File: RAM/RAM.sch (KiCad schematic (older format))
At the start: 27 parts, among them J1 Conn_01x08_Male, J2 Conn_01x08_Male, J3 Conn_01x08_Male, J4 Conn_01x05_Male, J5 Conn_01x08_Male, U1 74LS283, U2 CY62256-70PC, U3 74LS283, U4 74LS283, U5 74LS283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

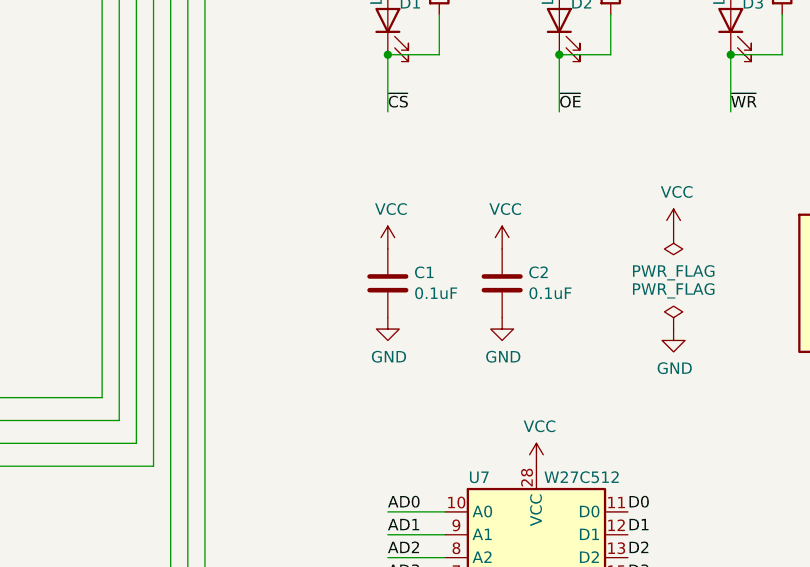
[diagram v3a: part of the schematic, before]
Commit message: Polishing RAM & ROM
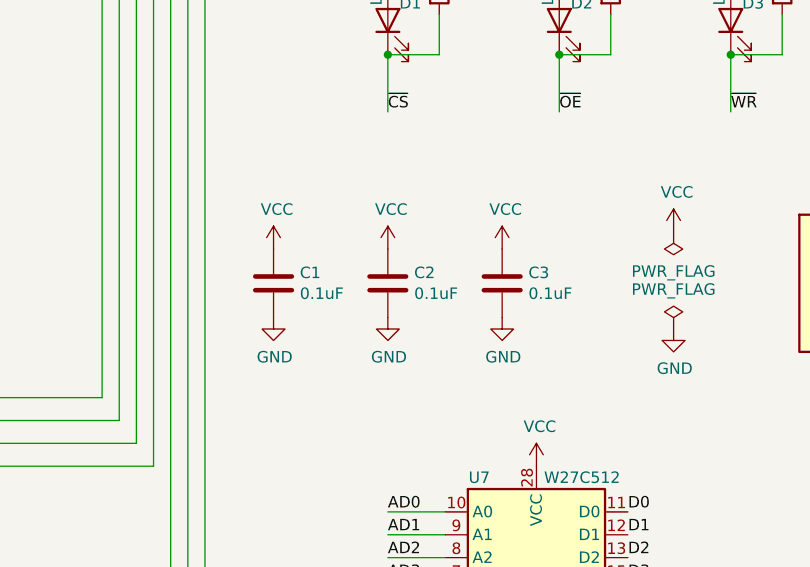
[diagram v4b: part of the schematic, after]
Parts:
- added C3: 0.1uF, Capacitor_THT:C_Disc_D7.5mm_W5.0mm_P10.00mm, symbol Device:C
- C1: footprint Resistor_SMD:R_0805_2012Metric_Pad1.20x1.40mm_HandSolder -> Capacitor_THT:C_Disc_D7.5mm_W5.0mm_P10.00mm
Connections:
- net GND: now also C3.2
- net VCC: now also C3.1
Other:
- moved on the sheet: C1, C2
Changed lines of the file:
@@
 L power:VCC #PWR012
 U 1 1 63DCFBC2
-P 5000 5100
-F 0 "#PWR012" H 5000 4950 50  0001 C CNN
-F 1 "VCC" H 5015 5273 50  0000 C CNN
-F 2 "" H 5000 5100 50  0001 C CNN
-F 3 "" H 5000 5100 50  0001 C CNN
-	1    5000 5100
+P 4500 5100
+F 0 "#PWR012" H 4500 4950 50  0001 C CNN
+F 1 "VCC" H 4515 5273 50  0000 C CNN
+F 2 "" H 4500 5100 50  0001 C CNN
+F 3 "" H 4500 5100 50  0001 C CNN
+	1    4500 5100
 	1    0    0    -1
 $EndComp
@@
 L power:GND #PWR013
 U 1 1 63DD055E
-P 5000 5400
-F 0 "#PWR013" H 5000 5150 50  0001 C CNN
-F 1 "GND" H 5005 5227 50  0000 C CNN
-F 2 "" H 5000 5400 50  0001 C CNN
-F 3 "" H 5000 5400 50  0001 C CNN
-	1    5000 5400
+P 4500 5400
+F 0 "#PWR013" H 4500 5150 50  0001 C CNN
+F 1 "GND" H 4505 5227 50  0000 C CNN
+F 2 "" H 4500 5400 50  0001 C CNN
+F 3 "" H 4500 5400 50  0001 C CNN
+	1    4500 5400
 	1    0    0    -1
 $EndComp
@@
 L Device:C C1
 U 1 1 63DD1002
-P 5000 5250
-F 0 "C1" H 5115 5296 50  0000 L CNN
-F 1 "0.1uF" H 5115 5205 50  0000 L CNN
-F 2 "Resistor_SMD:R_0805_2012Metric_Pad1.20x1.40mm_HandSolder" H 5038 5100 50  0001 C CNN
-F 3 "~" H 5000 5250 50  0001 C CNN
-	1    5000 5250
+P 4500 5250
+F 0 "C1" H 4615 5296 50  0000 L CNN
+F 1 "0.1uF" H 4615 5205 50  0000 L CNN
+F 2 "Capacitor_THT:C_Disc_D7.5mm_W5.0mm_P10.00mm" H 4538 5100 50  0001 C CNN
+F 3 "~" H 4500 5250 50  0001 C CNN
+	1    4500 5250
 	1    0    0    -1
 $EndComp
@@
 L power:VCC #PWR018
 U 1 1 63E17CDB
-P 5500 5100
-F 0 "#PWR018" H 5500 4950 50  0001 C CNN
-F 1 "VCC" H 5515 5273 50  0000 C CNN
-F 2 "" H 5500 5100 50  0001 C CNN
-F 3 "" H 5500 5100 50  0001 C CNN
-	1    5500 5100
+P 5000 5100
+F 0 "#PWR018" H 5000 4950 50  0001 C CNN
+F 1 "VCC" H 5015 5273 50  0000 C CNN
+F 2 "" H 5000 5100 50  0001 C CNN
+F 3 "" H 5000 5100 50  0001 C CNN
+	1    5000 5100
 	1    0    0    -1
 $EndComp
@@
 L power:GND #PWR019
 U 1 1 63E17CE1
-P 5500 5400
-F 0 "#PWR019" H 5500 5150 50  0001 C CNN
-F 1 "GND" H 5505 5227 50  0000 C CNN
-F 2 "" H 5500 5400 50  0001 C CNN
-F 3 "" H 5500 5400 50  0001 C CNN
-	1    5500 5400
+P 5000 5400
+F 0 "#PWR019" H 5000 5150 50  0001 C CNN
+F 1 "GND" H 5005 5227 50  0000 C CNN
+F 2 "" H 5000 5400 50  0001 C CNN
+F 3 "" H 5000 5400 50  0001 C CNN
+	1    5000 5400
 	1    0    0    -1
 $EndComp
@@
 L Device:C C2
 U 1 1 63E17CE7
-P 5500 5250
-F 0 "C2" H 5615 5296 50  0000 L CNN
-F 1 "0.1uF" H 5615 5205 50  0000 L CNN
-F 2 "Capacitor_THT:C_Disc_D7.5mm_W5.0mm_P10.00mm" H 5538 5100 50  0001 C CNN
-F 3 "~" H 5500 5250 50  0001 C CNN
-	1    5500 5250
+P 5000 5250
+F 0 "C2" H 5115 5296 50  0000 L CNN
+F 1 "0.1uF" H 5115 5205 50  0000 L CNN
+F 2 "Capacitor_THT:C_Disc_D7.5mm_W5.0mm_P10.00mm" H 5038 5100 50  0001 C CNN
+F 3 "~" H 5000 5250 50  0001 C CNN
+	1    5000 5250
 	1    0    0    -1
 $EndComp
@@
 Wire Wire Line
 	5375 9625 5375 9750
+$Comp
+L power:VCC #PWR025
+U 1 1 64941C0B
+P 5500 5100
+F 0 "#PWR025" H 5500 4950 50  0001 C CNN
+F 1 "VCC" H 5515 5273 50  0000 C CNN
+F 2 "" H 5500 5100 50  0001 C CNN
+F 3 "" H 5500 5100 50  0001 C CNN
+	1    5500 5100
+	1    0    0    -1
+$EndComp
+$Comp
+L power:GND #PWR026
+U 1 1 64941C11
+P 5500 5400
+F 0 "#PWR026" H 5500 5150 50  0001 C CNN
+F 1 "GND" H 5505 5227 50  0000 C CNN
+F 2 "" H 5500 5400 50  0001 C CNN
+F 3 "" H 5500 5400 50  0001 C CNN
+	1    5500 5400
+	1    0    0    -1
+$EndComp
+$Comp
+L Device:C C3
+U 1 1 64941C17
+P 5500 5250
+F 0 "C3" H 5615 5296 50  0000 L CNN
+F 1 "0.1uF" H 5615 5205 50  0000 L CNN
+F 2 "Capacitor_THT:C_Disc_D7.5mm_W5.0mm_P10.00mm" H 5538 5100 50  0001 C CNN
+F 3 "~" H 5500 5250 50  0001 C CNN
+	1    5500 5250
+	1    0    0    -1
+$EndComp
 $EndSCHEMATC

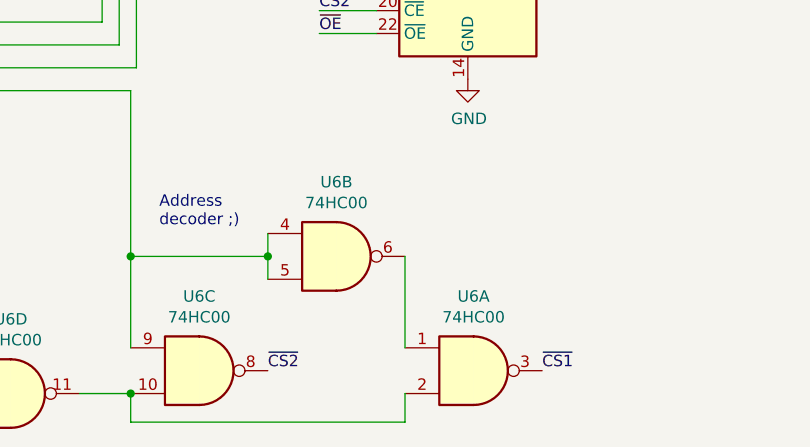
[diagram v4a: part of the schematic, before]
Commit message: Polishing RAM & ROM
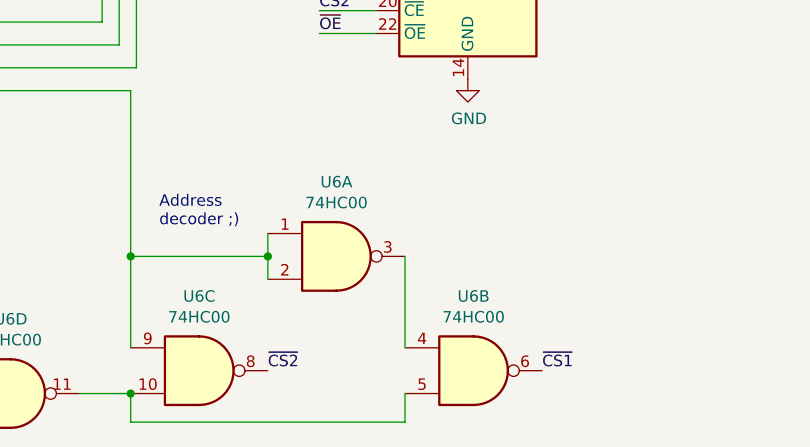
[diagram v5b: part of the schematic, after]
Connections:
- net ~CS1: now also U6.6; no longer U6.3
- net at U5.10 (S4), U6.9: now also U6.1, U6.2; no longer U6.4, U6.5
- net at U6.10, U6.11: now also U6.5; no longer U6.2
- new net: U6.3, U6.4
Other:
- moved on the sheet: U6A, U6B
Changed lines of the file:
@@
 L 74xx:74HC00 U6
 U 1 1 6495168F
+P 5075 9025
+F 0 "U6" H 5075 9350 50  0000 C CNN
+F 1 "74HC00" H 5075 9259 50  0000 C CNN
+F 2 "Package_DIP:DIP-14_W7.62mm" H 5075 9025 50  0001 C CNN
+F 3 "http://www.ti.com/lit/gpn/sn74hc00" H 5075 9025 50  0001 C CNN
+	1    5075 9025
+	1    0    0    -1
+$EndComp
+$Comp
+L 74xx:74HC00 U6
+U 2 1 64953C72
 P 5675 9525
 F 0 "U6" H 5675 9850 50  0000 C CNN
@@
 F 2 "Package_DIP:DIP-14_W7.62mm" H 5675 9525 50  0001 C CNN
 F 3 "http://www.ti.com/lit/gpn/sn74hc00" H 5675 9525 50  0001 C CNN
-	1    5675 9525
+	2    5675 9525
 	1    0    0    -1
 $EndComp
-$Comp
-L 74xx:74HC00 U6
-U 2 1 64953C72
-P 5075 9025
-F 0 "U6" H 5075 9350 50  0000 C CNN
-F 1 "74HC00" H 5075 9259 50  0000 C CNN
-F 2 "Package_DIP:DIP-14_W7.62mm" H 5075 9025 50  0001 C CNN
-F 3 "http://www.ti.com/lit/gpn/sn74hc00" H 5075 9025 50  0001 C CNN
-	2    5075 9025
-	1    0    0    -1
-$EndComp

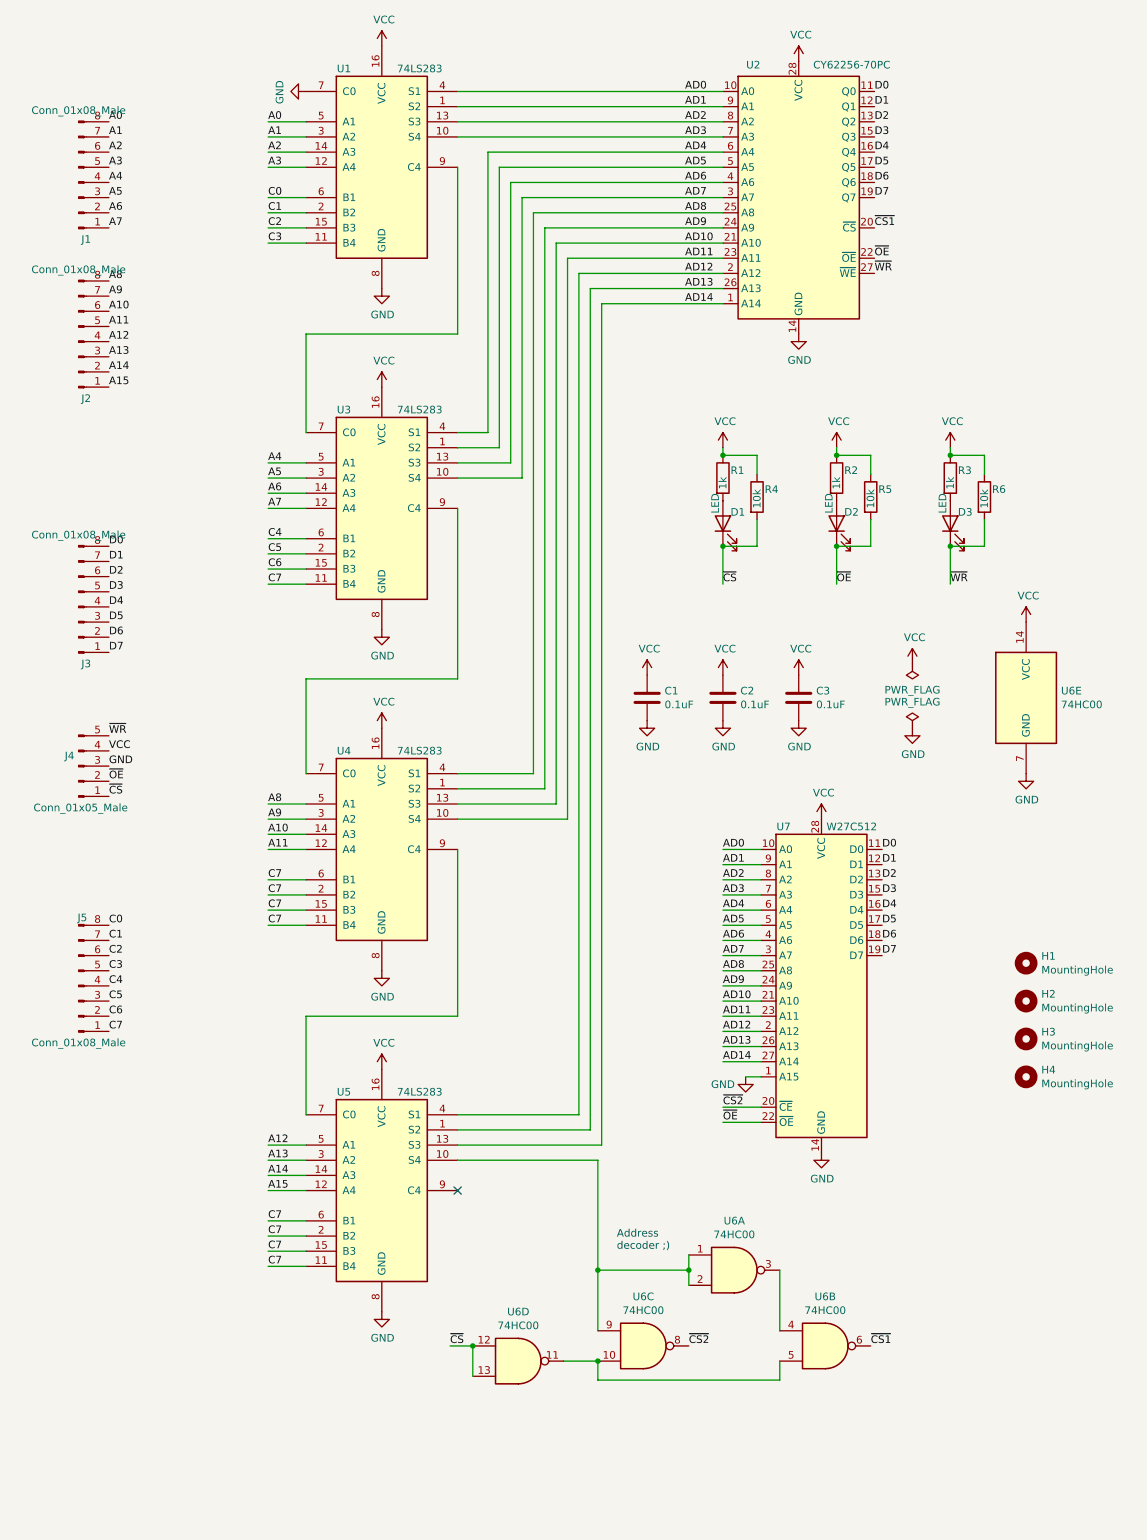
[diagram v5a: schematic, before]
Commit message: Add switch RAM/ROM
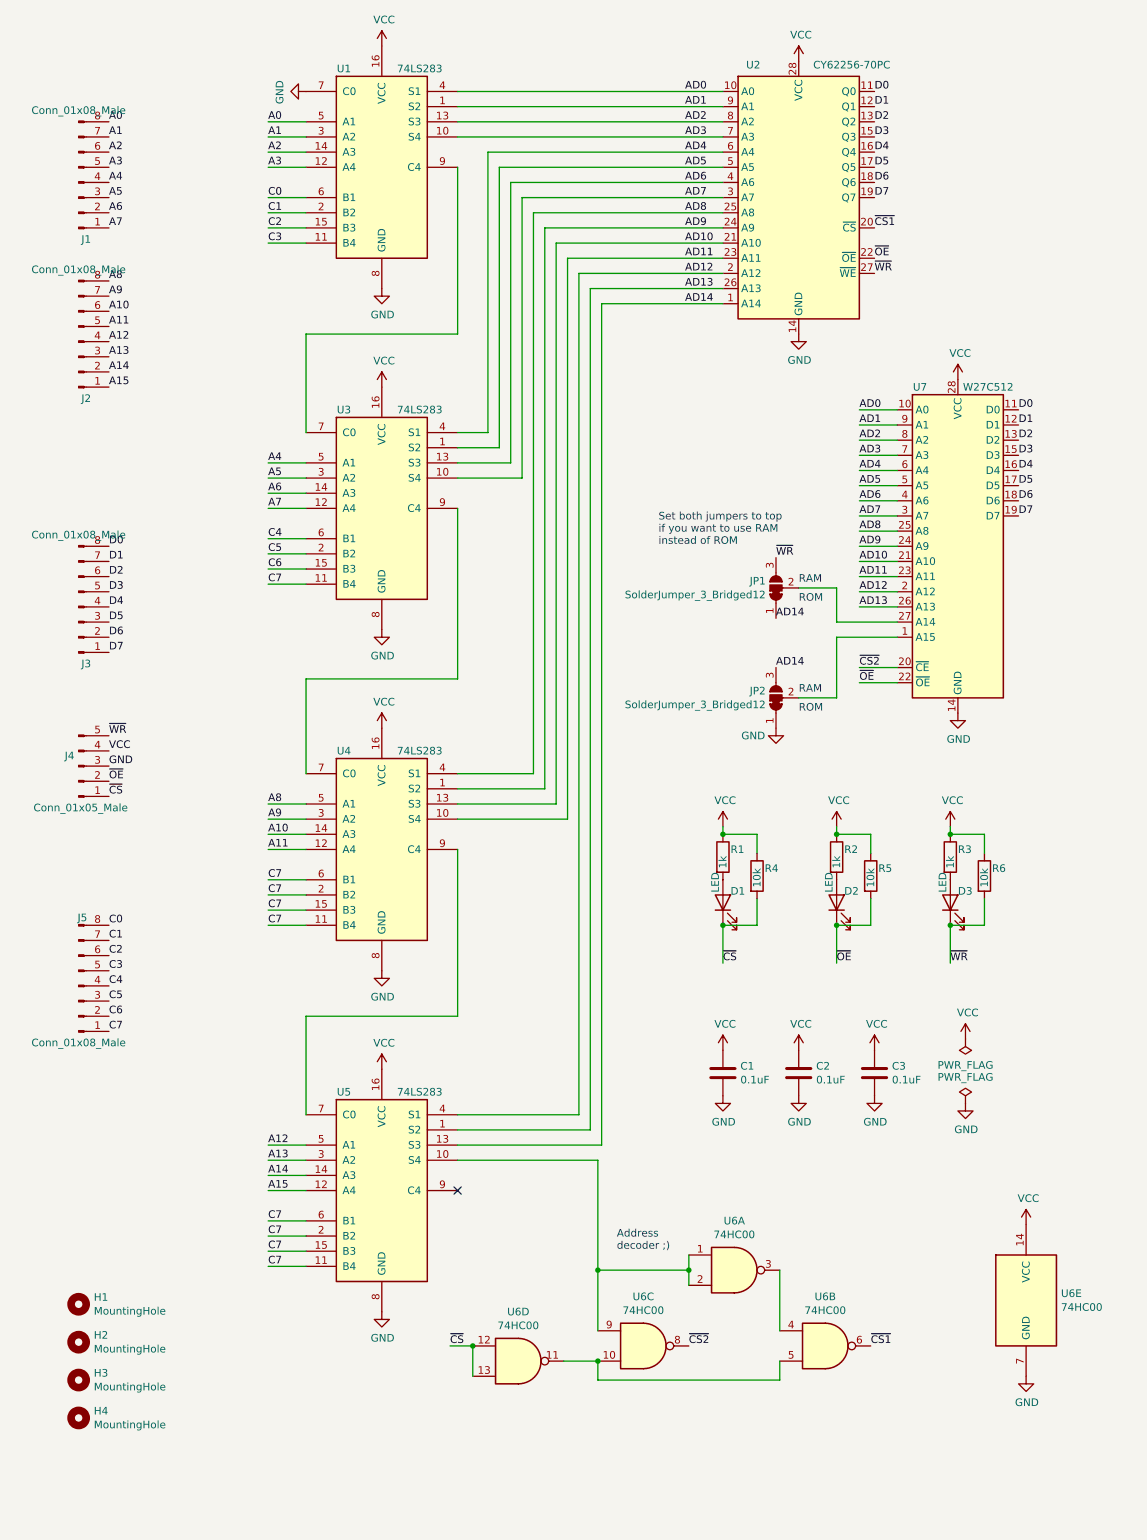
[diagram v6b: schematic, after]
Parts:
- added JP1, JP2: SolderJumper_3_Bridged12, Jumper:SolderJumper-3_P1.3mm_Open_Pad1.0x1.5mm_NumberLabels, symbol Jumper:SolderJumper_3_Bridged12
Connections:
- net AD14: now also JP1.1 (A), JP2.3 (B); no longer U7.27 (A14)
- net GND: now also JP2.1 (A); no longer U7.1 (A15)
- net ~WR: now also JP1.3 (B)
- new net: JP2.2 (C), U7.1 (A15)
- new net: JP1.2 (C), U7.27 (A14)
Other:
- note added: "RAM"
- note added: "ROM"
- note added: "Set both jumpers to top\nif you want to use RAM\ninstead of ROM"
- moved on the sheet: C1, C2, C3, D1, D2, D3, H1, H2, H3, H4, R1, R2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

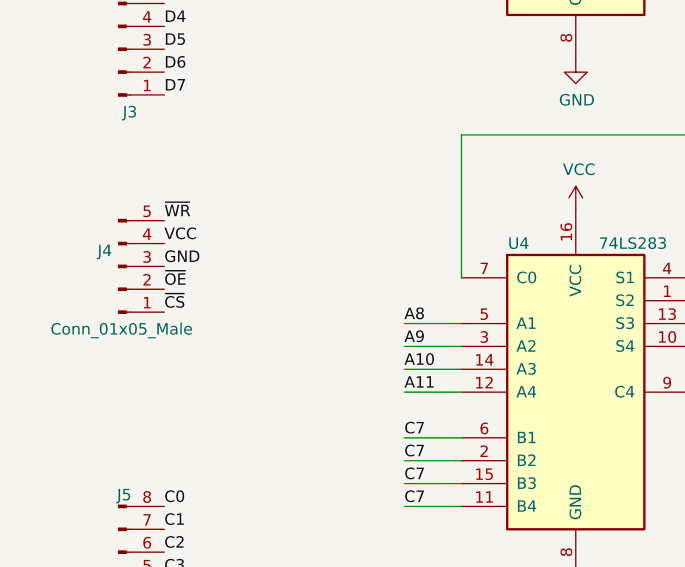
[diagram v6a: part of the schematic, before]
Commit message: RAM. Add reverse polarity protection.
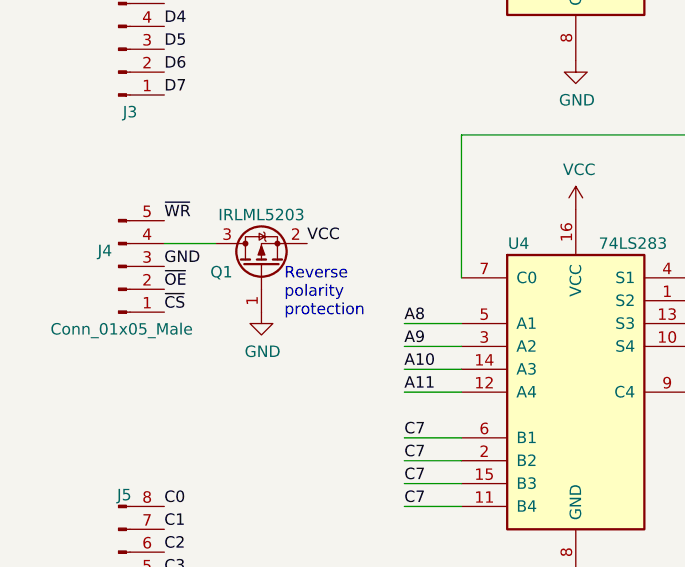
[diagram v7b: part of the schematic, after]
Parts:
- added Q1: IRLML5203, Package_TO_SOT_SMD:SOT-23, symbol Transistor_FET:IRLML5203
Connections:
- net GND: now also Q1.1 (G)
- net VCC: now also Q1.2 (S); no longer J4.4 (Pin_4)
- new net: J4.4 (Pin_4), Q1.3 (D)
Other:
- note added: "Reverse\npolarity\nprotection"
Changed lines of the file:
@@
 Text Label 950  5700 0    50   ~ 0
 GND
-Text Label 950  5600 0    50   ~ 0
+Text Label 1575 5600 0    50   ~ 0
 VCC
 Text Label 950  5500 0    50   ~ 0
@@
 Text Notes 4575 4250 0    50   ~ 0
 Set both jumpers to top\nif you want to use RAM\ninstead of ROM
+$Comp
+L Transistor_FET:IRLML5203 Q1
+U 1 1 64C0CC9D
+P 1375 5700
+F 0 "Q1" V 1350 5875 50  0000 C CNN
+F 1 "IRLML5203" V 1600 5700 50  0000 C CNN
+F 2 "Package_TO_SOT_SMD:SOT-23" H 1575 5625 50  0001 L CIN
+F 3 "https://www.infineon.com/dgdl/irlml5203pbf.pdf?fileId=5546d462533600a40153566868da261d" H 1375 5700 50  0001 L CNN
+	1    1375 5700
+	0    -1   -1   0
+$EndComp
+$Comp
+L power:GND #PWR0102
+U 1 1 64C0F060
+P 1375 5900
+F 0 "#PWR0102" H 1375 5650 50  0001 C CNN
+F 1 "GND" H 1380 5727 50  0000 C CNN
+F 2 "" H 1375 5900 50  0001 C CNN
+F 3 "" H 1375 5900 50  0001 C CNN
+	1    1375 5900
+	1    0    0    -1
+$EndComp
+Wire Wire Line
+	950  5600 1175 5600
+Text Notes 1475 5925 0    50   ~ 0
+Reverse\npolarity\nprotection
 $EndSCHEMATC
